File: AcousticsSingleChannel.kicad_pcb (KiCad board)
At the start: 4 copper layers, 25.4 x 25.4 mm, 51 parts, among them J1 Conn_01x04_Pin, J2 Conn_01x04_Pin, J4 Conn_01x09_Pin, U1 OPA1604AIPWR, U2 OPA1604AIPWR, U3 LTC6910-3CTS8#TRPBF, U4 ADS7042IDCUR

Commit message: tracks
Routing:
- net /G0_out: track 13.7 -> 9.50 mm
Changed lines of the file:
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@@
 		(at 147.35806 115.492005 90)
 		(property "Reference" "R7"
-			(at -0.762 -1.651 90)
+			(at -0.635 -1.651 90)
 			(unlocked yes)
 			(layer "F.SilkS")
@@
 		(at 145.80506 107.573005 180)
 		(property "Reference" "R13"
-			(at -1.299 0.971 270)
+			(at -0.918 -0.299 0)
 			(unlocked yes)
 			(layer "F.SilkS")
@@
 		(at 130.37006 103.935005 90)
 		(property "Reference" "D2"
-			(at 1.27 -0.762 0)
+			(at 1.651 -1.046 0)
 			(unlocked yes)
 			(layer "F.SilkS")
@@
 		(at 132.52906 103.173005 90)
 		(property "Reference" "R21"
-			(at -1.778 -1.27 0)
+			(at 1.016 -0.919 0)
 			(unlocked yes)
 			(layer "F.SilkS")
@@
 		(at 149.34706 104.062005 90)
 		(property "Reference" "U3"
-			(at 0.3 1.454 0)
+			(at 1.143 2.075 0)
 			(unlocked yes)
 			(layer "F.SilkS")
@@
 		(at 143.90006 105.160005 90)
 		(property "Reference" "C8"
-			(at -0.508 0.889 180)
+			(at -0.508 1.426 0)
 			(unlocked yes)
 			(layer "F.SilkS")
@@
 		(at 140.14906 106.488005 180)
 		(property "Reference" "C1"
-			(at 2.159 0.648 0)
+			(at 0.792 1.537 0)
 			(unlocked yes)
 			(layer "F.SilkS")
@@
 		(at 143.90006 103.128005 -90)
 		(property "Reference" "R17"
-			(at -1.397 2.286 270)
+			(at -1.098 1.241 0)
 			(unlocked yes)
 			(layer "F.SilkS")
@@
 		(at 136.33906 117.016005 -90)
 		(property "Reference" "R3"
-			(at -0.762 0.635 0)
+			(at 1.905 0.665 0)
 			(unlocked yes)
 			(layer "F.SilkS")
@@
 		(at 135.19606 103.554005 180)
 		(property "Reference" "R25"
-			(at -0.93915 0.76933 270)
+			(at 1.173 1.651 0)
 			(unlocked yes)
 			(layer "F.SilkS")
@@
 		(at 153.32706 113.714005 180)
 		(property "Reference" "C6"
-			(at 0.127 1.27 90)
+			(at 0.889 2.032 0)
 			(unlocked yes)
 			(layer "F.SilkS")
@@
 		(at 150.53306 117.270005 90)
 		(property "Reference" "R11"
-			(at -0.127 1.27 0)
+			(at -0.381 1.397 0)
 			(unlocked yes)
 			(layer "F.SilkS")
@@
 		(at 143.04006 115.619005 90)
 		(property "Reference" "C7"
-			(at -1.778 -1.397 90)
+			(at -0.254 -3.429 0)
 			(unlocked yes)
 			(layer "F.SilkS")
@@
 		)
 		(property "Value" "5005"
-			(at 3.2832 2.4064 0)
+			(at 0.254 -2.413 0)
 			(layer "F.Fab")
 			(effects
@@
 		(at 139.38706 117.016005 90)
 		(property "Reference" "R16"
-			(at 1.143 -0.889 0)
+			(at -1.778 -1.046 0)
 			(unlocked yes)
 			(layer "F.SilkS")
@@
 		(at 133.29106 117.016005 -90)
 		(property "Reference" "R1"
-			(at -0.889 1.016 0)
+			(at 1.905 0.792 0)
 			(unlocked yes)
 			(layer "F.SilkS")
@@
 		(at 143.51906 108.208005)
 		(property "Reference" "C10"
-			(at -1.524 -1.156 270)
+			(at -1.495 -1.479 0)
 			(unlocked yes)
 			(layer "F.SilkS")
@@
 		(at 130.62406 109.396005 180)
 		(property "Reference" "C3"
-			(at 0.127 1.143 90)
+			(at 1.173 1.524 0)
 			(unlocked yes)
 			(layer "F.SilkS")
@@
 		(at 132.40206 109.396005 180)
 		(property "Reference" "C5"
-			(at 0.508 1.397 0)
+			(at 0.919 1.524 0)
 			(unlocked yes)
 			(layer "F.SilkS")
@@
 		(at 143.16706 117.143005 90)
 		(property "Reference" "C9"
-			(at -0.889 2.286 90)
+			(at -1.778 -0.762 0)
 			(unlocked yes)
 			(layer "F.SilkS")
@@
 		(at 150.53306 115.492005 -90)
 		(property "Reference" "C4"
-			(at 0.381 -1.397 0)
+			(at 0.635 -1.778 0)
 			(unlocked yes)
 			(layer "F.SilkS")
@@
 		(at 130.62406 116.889005)
 		(property "Reference" "R9"
-			(at 0.732 1.905 0)
+			(at -0.665 2.667 0)
 			(unlocked yes)
 			(layer "F.SilkS")
@@
 	)
 	(segment
-		(start 153.32706 99.236005)
-		(end 153.32706 101.395005)
+		(start 150.40606 102.668005)
+		(end 150.40606 98.474005)
 		(width 0.254)
 		(layer "F.Cu")
@@
 	)
 	(segment
-		(start 146.59606 99.500165)
-		(end 148.25722 97.839005)
+		(start 146.59606 98.601005)
+		(end 146.59606 99.500165)
 		(width 0.254)
 		(layer "F.Cu")
@@
 	)
 	(segment
-		(start 148.25722 97.839005)
-		(end 151.93006 97.839005)
+		(start 149.89806 97.966005)
+		(end 147.23106 97.966005)
 		(width 0.254)
 		(layer "F.Cu")
@@
 	)
 	(segment
-		(start 153.32706 101.395005)
-		(end 151.97006 102.752005)
+		(start 150.40606 98.474005)
+		(end 149.89806 97.966005)
 		(width 0.254)
 		(layer "F.Cu")
@@
 	)
 	(segment
-		(start 151.93006 97.839005)
-		(end 153.32706 99.236005)
+		(start 150.32206 102.752005)
+		(end 150.40606 102.668005)
 		(width 0.254)
 		(layer "F.Cu")
@@
 	)
 	(segment
-		(start 151.97006 102.752005)
-		(end 150.32206 102.752005)
+		(start 147.23106 97.966005)
+		(end 146.59606 98.601005)
 		(width 0.254)
 		(layer "F.Cu")
@@
 	)
 	(segment
-		(start 150.5229 98.347005)
-		(end 148.396514 98.347005)
+		(start 151.42206 103.935005)
+		(end 149.34106 103.935005)
 		(width 0.254)
 		(layer "F.Cu")
@@
 	)
 	(segment
-		(start 151.67606 99.500165)
-		(end 150.5229 98.347005)
+		(start 152.52606 102.831005)
+		(end 151.42206 103.935005)
 		(width 0.254)
 		(layer "F.Cu")
@@
 	)
 	(segment
-		(start 147.99306 98.750459)
-		(end 147.99306 100.911209)
+		(start 151.67606 99.500165)
+		(end 152.52606 100.350165)
 		(width 0.254)
 		(layer "F.Cu")
@@
 	)
 	(segment
-		(start 147.99306 100.911209)
-		(end 149.02206 101.940209)
+		(start 149.34106 103.935005)
+		(end 149.02206 103.616005)
 		(width 0.254)
 		(layer "F.Cu")
@@
 	)
 	(segment
-		(start 148.396514 98.347005)
-		(end 147.99306 98.750459)
+		(start 152.52606 100.350165)
+		(end 152.52606 102.831005)
 		(width 0.254)
 		(layer "F.Cu")
@@
 	)
 	(segment
-		(start 149.02206 101.940209)
+		(start 149.02206 103.616005)
 		(end 149.02206 102.752005)
 		(width 0.254)

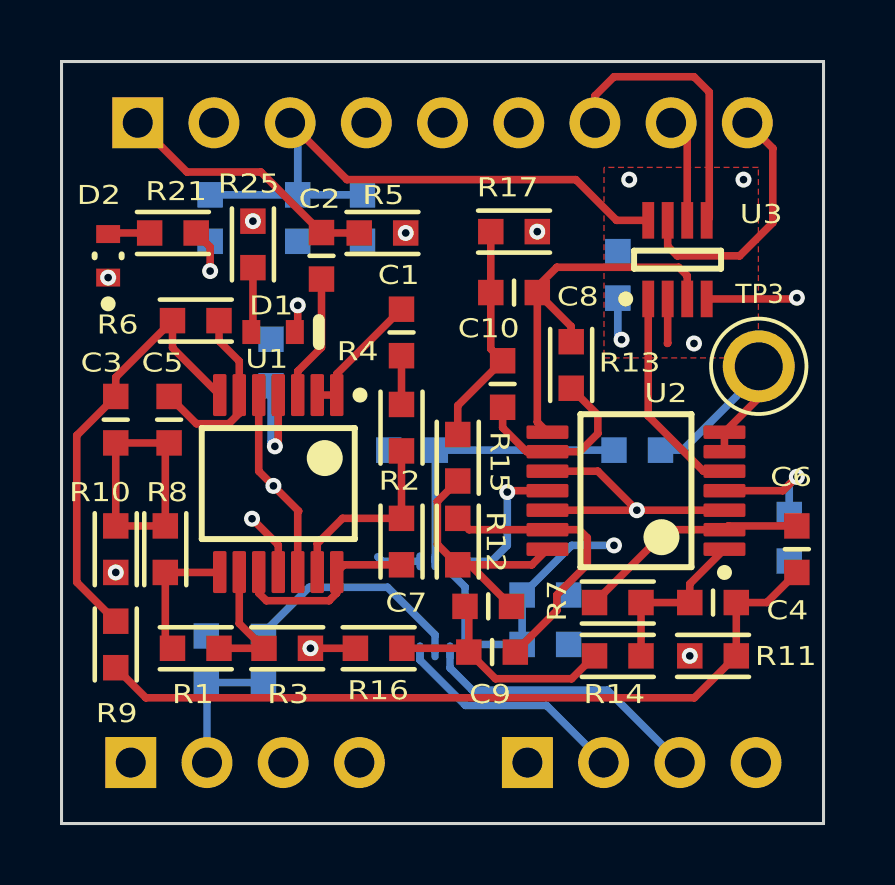
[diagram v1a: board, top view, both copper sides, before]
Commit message: Changed pinouts causing minor changes to layer1 layout.
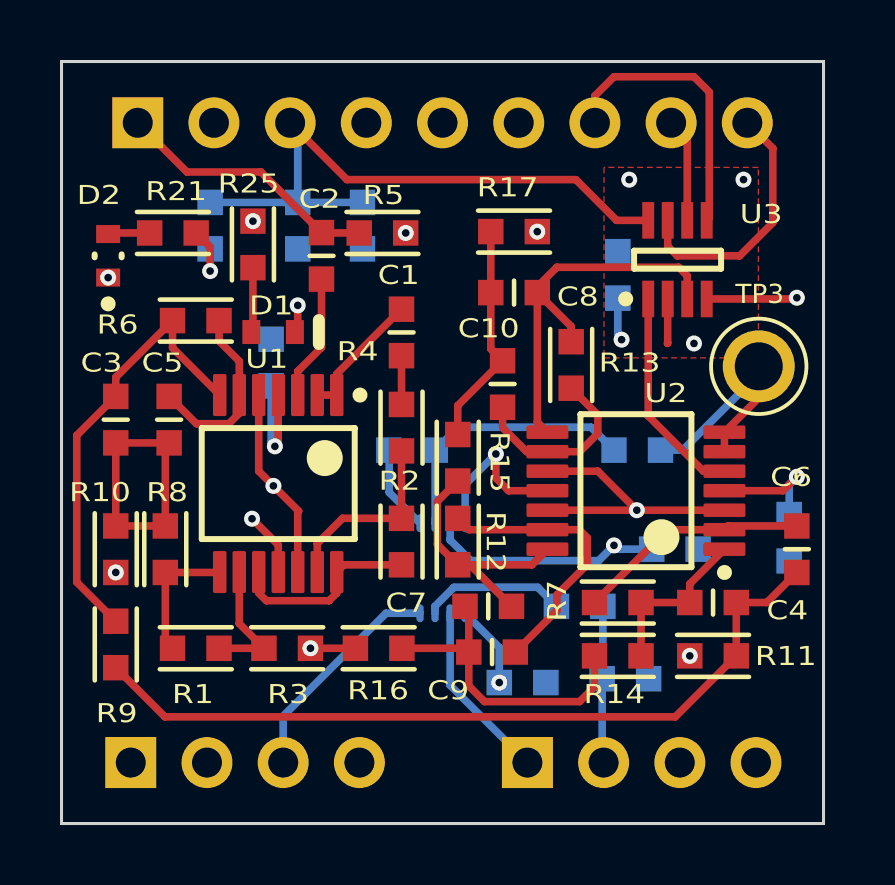
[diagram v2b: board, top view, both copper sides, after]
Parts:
- moved R27 14.0 mm to (147.6, 118.0), turned to 90 degrees
- moved R26 10.7 mm to (146.1, 115.6), turned to 90 degrees
- moved C18 5.36 mm to (149.3, 113.7)
- moved C13 3.02 mm to (144.2, 118.2)
- moved U4 1.27 mm to (141.5, 114.3)
- moved C12 0.25 mm to (136.7, 102.9)
- moved C14 0.25 mm to (138.8, 102.9)
- moved C15 0.25 mm to (133.8, 102.9)
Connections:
- J1 pad 2: Net-(J1-Pin_2) -> /RESET
- J1 pad 3: /RESET -> /CS
- J2 pad 1: /START -> /SCLK
- J2 pad 2: /CS -> Net-(J2-Pin_2)
- J2 pad 3: /SCLK -> /CLK
- J2 pad 4: /CLK -> /START
- R26 pad 1: Net-(J1-Pin_2) -> Net-(J2-Pin_2)
- R27 pad 2: Net-(J1-Pin_2) -> Net-(J2-Pin_2)
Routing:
- net Net-(J2-Pin_2): track 0.00 -> 5.24 mm
- net Net-(J1-Pin_2): track 4.59 -> 0.00 mm
- net /SCLK: track 9.52 -> 6.05 mm
- net /DOUT: track 7.67 -> 4.81 mm
- net GND: track 12.4 -> 14.5 mm
- net /Band Pass Filter/F3_In: track 8.73 -> 10.6 mm
- net Net-(U4-AINP): track 9.67 -> 9.03 mm
- net /Band Pass Filter/F2_In: track 25.9 -> 26.4 mm
- net +3.3V: track 39.4 -> 39.6 mm, vias 4 -> 5

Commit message: Layer Stackup Updates.
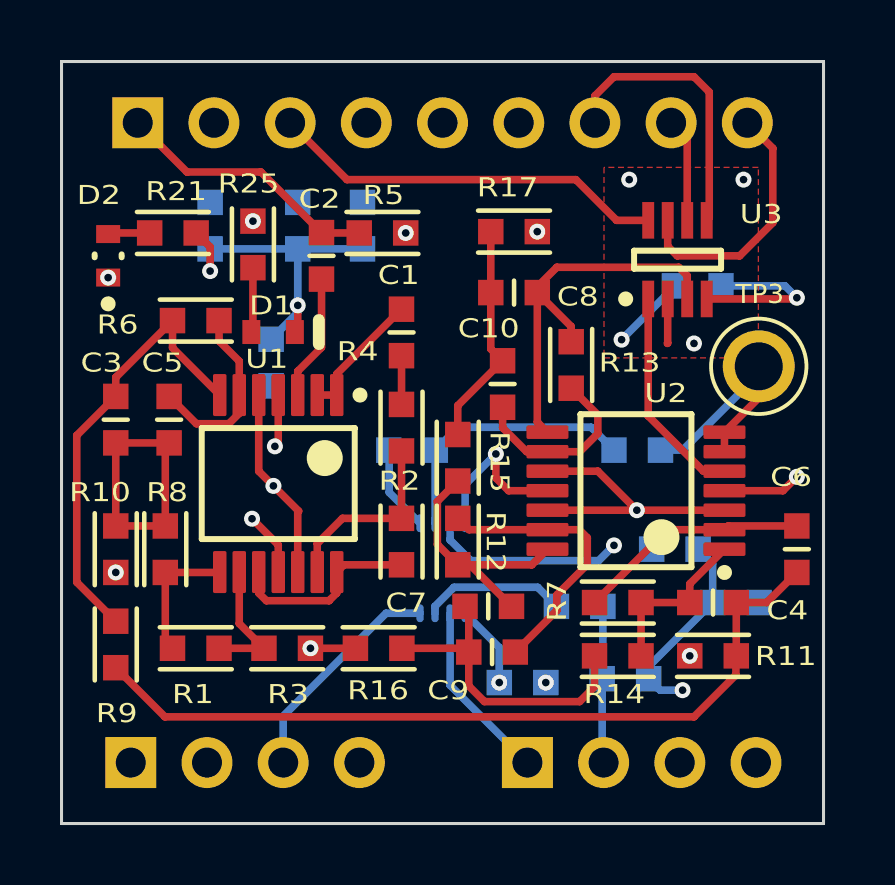
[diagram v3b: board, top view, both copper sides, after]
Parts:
- moved C16 2.80 mm to (151.3, 115.5), turned to -90 degrees
- moved C11 2.69 mm to (150.0, 104.9), turned to -90 degrees
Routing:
- net GND: track 14.5 -> 32.3 mm, vias 5 -> 7
- net +3.3V: track 39.6 -> 27.4 mm
- net AGND: track 20.3 -> 21.4 mm
- added copper zone on B.Cu, net +3.3V
- added copper zone on In1.Cu, net GND
- removed copper zone on In1.Cu, net +3.3V
- removed copper zone on B.Cu, net GND
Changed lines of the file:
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@@
 	(footprint "AltiumImports:SMD-0603C"
 		(layer "B.Cu")
-		(at 147.35806 104.570005)
+		(at 150.02198 104.936925 -90)
 		(property "Reference" "C11"
-			(at 1.524 -1.524 0)
+			(at -0.875 -0.775 0)
 			(unlocked yes)
 			(layer "B.SilkS")
@@
 		)
 		(property "Value" "1µF"
-			(at 4.69437 2.11968 180)
+			(at 4.69437 2.11968 90)
 			(unlocked yes)
 			(layer "B.SilkS")
@@
 		)
 		(property "Datasheet" ""
-			(at 0 0 0)
+			(at 0 0 90)
 			(layer "B.Fab")
 			(hide yes)
@@
 		)
 		(property "Description" ""
-			(at 0 0 0)
+			(at 0 0 90)
 			(layer "B.Fab")
 			(hide yes)
@@
 		)
 		(property "Part Number" "GCM188R71C105KA64D"
-			(at 0 0 180)
+			(at 0 0 90)
 			(unlocked yes)
 			(layer "B.Fab")
@@
 		)
 		(pad "1" smd rect
-			(at 0 0.775 90)
+			(at 0 0.775)
 			(size 0.85 0.85)
 			(layers "B.Cu" "B.Mask" "B.Paste")
@@
 		)
 		(pad "2" smd rect
-			(at 0 -0.775 90)
+			(at 0 -0.775)
 			(size 0.85 0.85)
 			(layers "B.Cu" "B.Mask" "B.Paste")
@@
 	(footprint "AltiumImports:SMD-0603C"
 		(layer "B.Cu")
-		(at 153.07306 113.333005)
+		(at 151.29506 115.492005 -90)
 		(property "Reference" "C16"
-			(at -1.397 1.143 270)
+			(at -0.889 -2.032 0)
 			(unlocked yes)
 			(layer "B.SilkS")
@@
 		)
 		(property "Value" "1µF"
-			(at 6.58797 -2.3844 0)
+			(at 6.58797 -2.3844 270)
 			(unlocked yes)
 			(layer "B.SilkS")
@@
 		)
 		(property "Datasheet" ""
-			(at 0 0 0)
+			(at 0 0 90)
 			(layer "B.Fab")
 			(hide yes)
@@
 		)
 		(property "Description" ""
-			(at 0 0 0)
+			(at 0 0 90)
 			(layer "B.Fab")
 			(hide yes)
@@
 		)
 		(property "Part Number" "CL10A105KA8NNNC"
-			(at 303.87032 -184.47303 0)
+			(at 303.87032 -184.47303 90)
 			(layer "B.Fab")
 			(hide yes)
@@
 		)
 		(pad "1" smd rect
-			(at 0 0.775 90)
+			(at 0 0.775)
 			(size 0.85 0.85)
 			(layers "B.Cu" "B.Mask" "B.Paste")
@@
 		)
 		(pad "2" smd rect
-			(at 0 -0.775 90)
+			(at 0 -0.775)
 			(size 0.85 0.85)
 			(layers "B.Cu" "B.Mask" "B.Paste")
@@
 	)
 	(via
+		(at 144.95806 118.159005)
+		(size 0.5334)
+		(drill 0.254)
+		(layers "F.Cu" "B.Cu")
+		(net 1)
+	)
+	(via
 		(at 135.16606 112.698005)
 		(size 0.5334)
@@
 	)
 	(via
+		(at 149.51706 118.413005)
+		(size 0.5334)
+		(drill 0.254)
+		(layers "F.Cu" "B.Cu")
+		(net 1)
+	)
+	(via
 		(at 153.32706 105.332005)
 		(size 0.5334)
@@
 	)
 	(segment
+		(start 149.51706 118.413005)
+		(end 148.76806 118.413005)
+		(width 0.254)
+		(layer "B.Cu")
+		(net 1)
+	)
+	(segment
+		(start 148.38706 117.625005)
+		(end 148.38706 118.032005)
+		(width 0.254)
+		(layer "B.Cu")
+		(net 1)
+	)
+	(segment
+		(start 150.52006 115.492005)
+		(end 148.38706 117.625005)
+		(width 0.254)
+		(layer "B.Cu")
+		(net 1)
+	)
+	(segment
+		(start 150.52006 114.196005)
+		(end 150.03806 113.714005)
+		(width 0.254)
+		(layer "B.Cu")
+		(net 1)
+	)
+	(segment
+		(start 150.52006 115.492005)
+		(end 150.52006 114.196005)
+		(width 0.254)
+		(layer "B.Cu")
+		(net 1)
+	)
+	(segment
+		(start 136.69006 105.586005)
+		(end 136.69006 105.827005)
+		(width 0.254)
+		(layer "B.Cu")
+		(net 1)
+	)
+	(segment
 		(start 142.266061 112.849005)
 		(end 142.266061 111.567004)
@@
 	)
 	(segment
+		(start 152.93198 104.936925)
+		(end 153.32706 105.332005)
+		(width 0.254)
+		(layer "B.Cu")
+		(net 1)
+	)
+	(segment
+		(start 136.69006 103.704165)
+		(end 133.76906 103.704165)
+		(width 0.254)
+		(layer "B.Cu")
+		(net 1)
+	)
+	(segment
+		(start 138.84906 103.704165)
+		(end 136.69006 103.704165)
+		(width 0.254)
+		(layer "B.Cu")
+		(net 1)
+	)
+	(segment
 		(start 142.266061 111.567004)
 		(end 143.29406 110.539005)
@@
 	)
 	(segment
+		(start 150.79698 104.936925)
+		(end 152.93198 104.936925)
+		(width 0.254)
+		(layer "B.Cu")
+		(net 1)
+	)
+	(segment
+		(start 148.76806 118.413005)
+		(end 148.38706 118.032005)
+		(width 0.254)
+		(layer "B.Cu")
+		(net 1)
+	)
+	(segment
 		(start 140.766062 112.849005)
 		(end 139.73806 111.821003)
@@
 	)
 	(segment
+		(start 136.69006 103.704165)
+		(end 136.69006 105.586005)
+		(width 0.254)
+		(layer "B.Cu")
+		(net 1)
+	)
+	(segment
+		(start 136.69006 105.827005)
+		(end 135.80106 106.716005)
+		(width 0.254)
+		(layer "B.Cu")
+		(net 1)
+	)
+	(segment
 		(start 135.87956 111.603505)
 		(end 136.72006 112.444005)
@@
 	)
 	(segment
-		(start 147.35806 105.345005)
-		(end 147.35806 106.602005)
+		(start 149.24698 104.967085)
+		(end 147.48506 106.729005)
 		(width 0.254)
 		(layer "B.Cu")
@@
 	)
 	(segment
-		(start 147.35806 106.602005)
-		(end 147.48506 106.729005)
+		(start 149.24698 104.936925)
+		(end 149.24698 104.967085)
 		(width 0.254)
 		(layer "B.Cu")
@@
 	(segment
 		(start 151.30806 117.270005)
+		(end 151.29506 117.283005)
+		(width 0.254)
+		(layer "F.Cu")
+		(net 15)
+	)
+	(segment
+		(start 151.30806 117.270005)
 		(end 151.30806 115.492005)
 		(width 0.254)
@@
 	)
 	(segment
-		(start 151.30806 115.492005)
-		(end 152.32406 115.492005)
+		(start 151.29506 117.905005)
+		(end 149.89806 119.302005)
 		(width 0.254)
 		(layer "F.Cu")
@@
 	)
 	(segment
-		(start 151.30806 117.270005)
-		(end 149.27606 119.302005)
+		(start 149.89806 119.302005)
+		(end 132.26206 119.302005)
 		(width 0.254)
 		(layer "F.Cu")
@@
 	)
 	(segment
-		(start 132.26206 119.302005)
-		(end 130.62406 117.664005)
+		(start 151.30806 115.492005)
+		(end 152.32406 115.492005)
 		(width 0.254)
 		(layer "F.Cu")
@@
 	)
 	(segment
-		(start 149.27606 119.302005)
-		(end 132.26206 119.302005)
+		(start 132.26206 119.302005)
+		(end 130.62406 117.664005)
+		(width 0.254)
+		(layer "F.Cu")
+		(net 15)
+	)
+	(segment
+		(start 151.29506 117.283005)
+		(end 151.29506 117.905005)
 		(width 0.254)
 		(layer "F.Cu")
@@
 	)
 	(segment
-		(start 153.07306 112.558005)
-		(end 153.07306 111.555005)
-		(width 0.254)
-		(layer "B.Cu")
-		(net 21)
-	)
-	(segment
-		(start 153.07306 111.555005)
-		(end 153.32706 111.301005)
-		(width 0.254)
-		(layer "B.Cu")
-		(net 21)
-	)
-	(segment
 		(start 143.40806 116.991004)
 		(end 142.266061 115.849005)
@@
 	)
 	(segment
-		(start 135.80106 110.158005)
-		(end 135.92806 110.285005)
-		(width 0.254)
-		(layer "B.Cu")
-		(net 21)
-	)
-	(segment
-		(start 138.84906 102.154165)
-		(end 136.69006 102.154165)
-		(width 0.254)
-		(layer "B.Cu")
-		(net 21)
-	)
-	(segment
 		(start 146.72306 114.095005)
 		(end 147.23106 113.587005)
@@
 	)
 	(segment
-		(start 135.80106 108.266005)
-		(end 135.80106 110.158005)
-		(width 0.254)
-		(layer "B.Cu")
-		(net 21)
-	)
-	(segment
-		(start 136.69006 102.154165)
-		(end 133.76906 102.154165)
-		(width 0.254)
-		(layer "B.Cu")
-		(net 21)
-	)
-	(segment
-		(start 148.48806 113.714005)
-		(end 147.35806 113.714005)
-		(width 0.254)
-		(layer "B.Cu")
-		(net 21)
-	)
-	(segment
-		(start 136.69006 102.154165)
-		(end 136.69006 99.754165)
-		(width 0.254)
-		(layer "B.Cu")
-		(net 21)
-	)
-	(segment
 		(start 142.458062 114.095005)
 		(end 146.72306 114.095005)
@@
 	)
 	(segment
-		(start 147.35806 113.714005)
-		(end 147.23106 113.587005)
-		(width 0.254)
-		(layer "B.Cu")
-		(net 21)
-	)
-	(segment
 		(start 141.766062 113.403005)
 		(end 142.458062 114.095005)
@@
 	)
 	(segment
-		(start 131.12492 120.826005)
-		(end 133.76906 118.181865)
+		(start 139.01906 104.443005)
+		(end 140.28906 103.173005)
 		(width 0.254)
 		(layer "In1.Cu")
@@
 	)
 	(segment
-		(start 139.01906 104.443005)
-		(end 140.28906 103.173005)
+		(start 131.12492 120.826005)
+		(end 133.76906 118.181865)
 		(width 0.254)
-		(layer "In1.Cu")
+		(layer "In2.Cu")
 		(net 34)
 	)
@@
 		(end 133.76906 104.443005)
 		(width 0.254)
-		(layer "In1.Cu")
+		(layer "In2.Cu")
 		(net 34)
 	)
@@
 	)
 	(zone
-		(net 1)
-		(net_name "GND")
+		(net 21)
+		(net_name "+3.3V")
 		(layer "B.Cu")
 		(hatch edge 0.5)
@@
 	)
 	(zone
-		(net 21)
-		(net_name "+3.3V")
+		(net 1)
+		(net_name "GND")
 		(layer "In1.Cu")
 		(hatch edge 0.5)
